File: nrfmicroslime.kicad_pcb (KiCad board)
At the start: 2 copper layers, 29.7 x 33 mm, 21 parts, among them J1 Conn_01x13_Pin, J2 Conn_01x13_Pin, J3 532610271, SW1 TS-1088-AR02016, U1 ICM-42688-V, U2 LIS2MDL, X1 S2D32.768KB20F30T

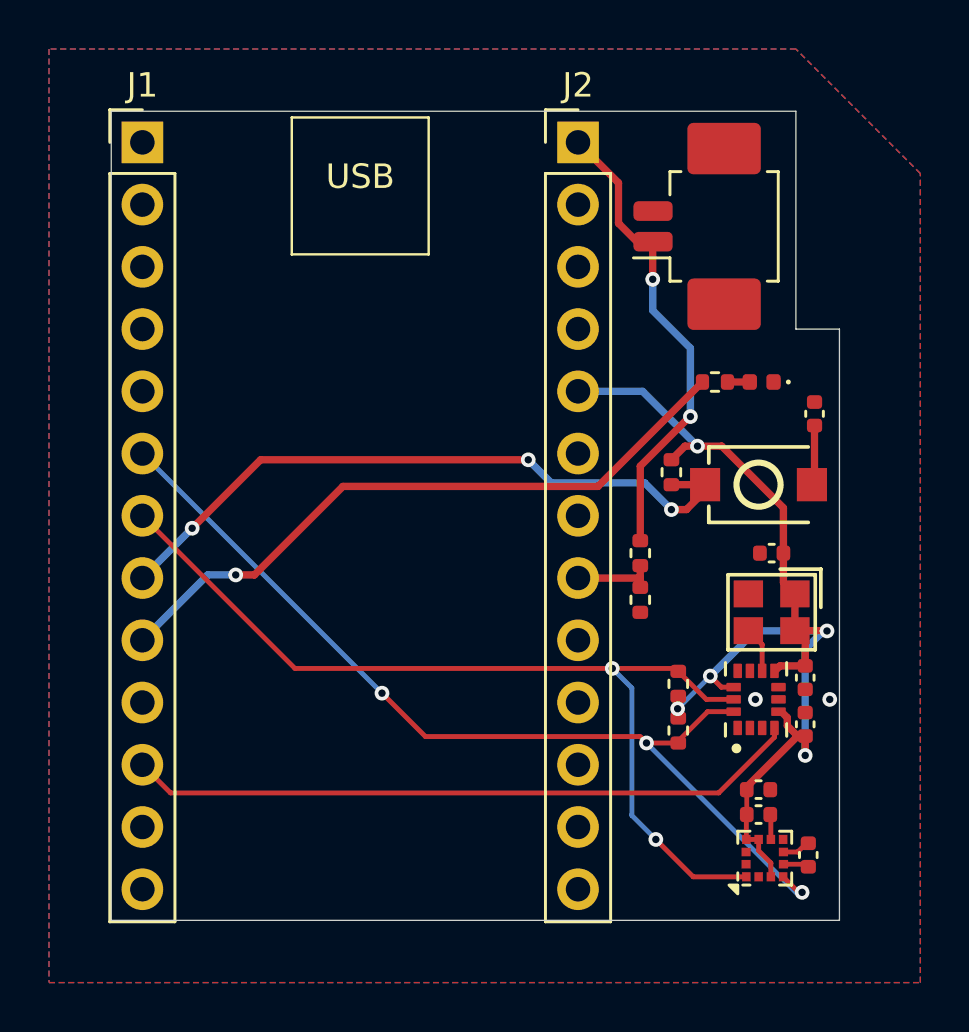
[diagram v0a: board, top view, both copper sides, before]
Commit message: narrower pcb, less components, pin configuration change
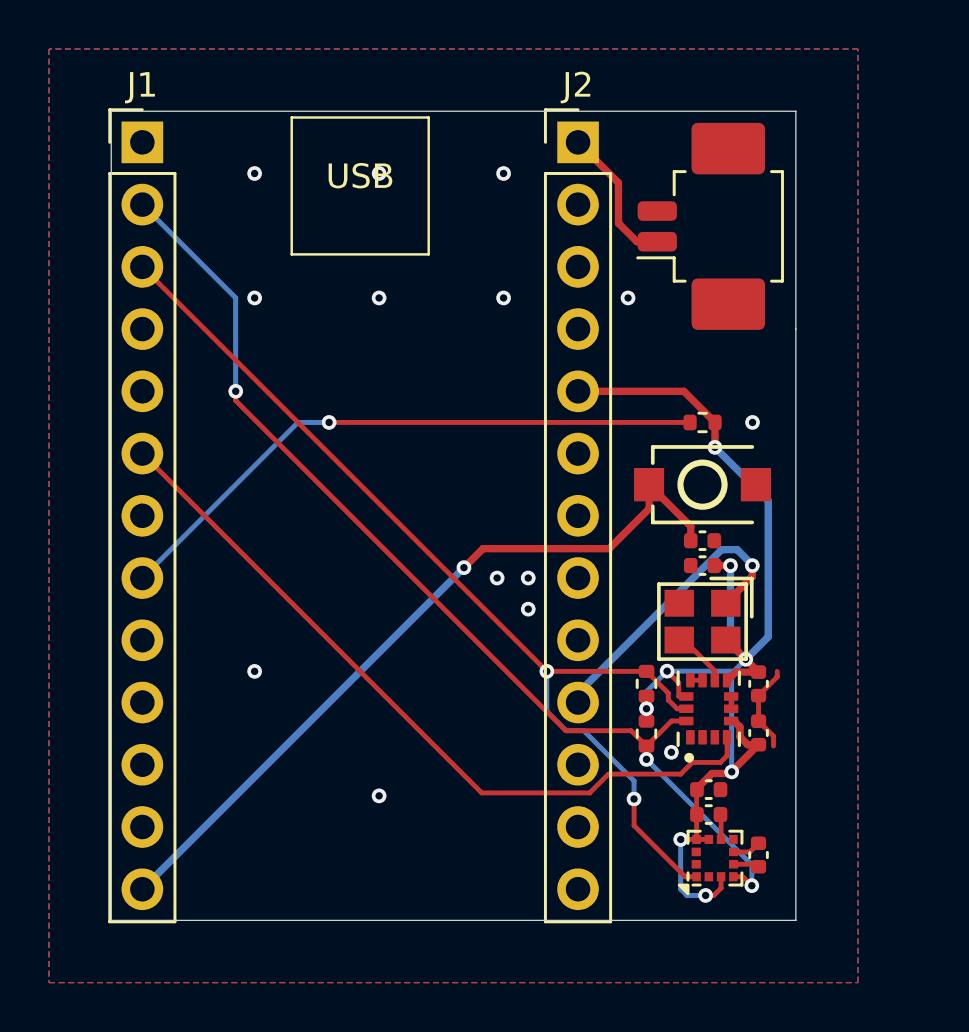
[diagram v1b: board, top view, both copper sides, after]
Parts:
- removed the C6 at (117.6, 45.4)
- removed LED1: NCD0402B1, LED_SMD:LED_0402_1005Metric
- removed the R2 at (113.5, 44.1)
- removed R3: 100k, Resistor_SMD:R_0402_1005Metric
- removed R6: 51k, Resistor_SMD:R_0402_1005Metric
- added C7: 100n, Capacitor_SMD:C_0402_1005Metric, F.Cu at (113.0, 50.5)
- U1: value ICM-42688-V -> ICM-42688-P
- moved C6 2.87 mm to (113.0, 51.6)
- moved X1 2.85 mm to (113.0, 53.8)
- moved R1 2.41 mm to (110.7, 58.4), turned to -90 degrees
- moved R1 2.40 mm to (113.0, 45.7), turned to 180 degrees
- moved R2 2.30 mm to (110.7, 56.4), turned to 90 degrees
- moved SW1 2.29 mm to (113.0, 48.3)
- moved C3 2.03 mm to (113.3, 61.7)
- moved C4 2.03 mm to (113.3, 60.7)
- moved C5 2.03 mm to (115.3, 63.4)
- moved U2 2.03 mm to (113.5, 63.5)
- moved U1 1.97 mm to (113.3, 57.4)
- moved C1 1.94 mm to (115.3, 58.4)
- moved C2 1.92 mm to (115.3, 56.4)
- moved J3 0.17 mm to (113.6, 37.7)
- renumbered C7 to C6, R4 to R1, R5 to R2
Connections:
- R1 pad 2: /0.20 -> /0.06
- R2 pad 2: /0.17 -> /0.08
- SW1 pad 1: /0.22 -> /1.06
- SW1 pad 2: Net-(C6-Pad1) -> GND
- U1 pad 13: /0.20 -> /0.08
- U1 pad 14: /0.17 -> /0.06
- U1 pad 4: /0.11 -> /0.17
- U2 pad 1: /0.20 -> /0.08
- U2 pad 4: /0.17 -> /0.06
- X1 pad 1: +3V3 -> /1.13
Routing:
- net /0.06: track 0.00 -> 42.6 mm, vias 0 -> 3
- net /0.08: track 0.00 -> 41.4 mm, vias 0 -> 2
- net /0.20: track 39.3 -> 0.00 mm, vias 2 -> 0
- net /1.06: track 0.00 -> 31.1 mm, vias 0 -> 1
- net /0.11: track 27.6 -> 0.00 mm
- net /0.24: track 27.2 -> 0.00 mm, vias 1 -> 0
- net +BATT: track 19.4 -> 5.73 mm, vias 2 -> 0
- net /1.13: track 0.00 -> 12.2 mm, vias 0 -> 1
- net /0.17: track 39.5 -> 31.0 mm, vias 3 -> 0
- net GND: track 2.19 -> 6.81 mm, vias 2 -> 14
- net /0.02: track 3.42 -> 0.00 mm
- net /0.22: track 28.1 -> 25.0 mm, vias 3 -> 1
- net +3V3: track 45.6 -> 48.4 mm, vias 5 -> 8
- net Net-(C6-Pad1): track 2.60 -> 0.00 mm
- net Net-(LED1-A): track 0.91 -> 0.00 mm
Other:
- board size 29.7 x 33 mm -> 27.9 x 33 mm
